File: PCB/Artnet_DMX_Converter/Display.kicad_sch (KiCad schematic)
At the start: 12 parts, among them J12 IDC

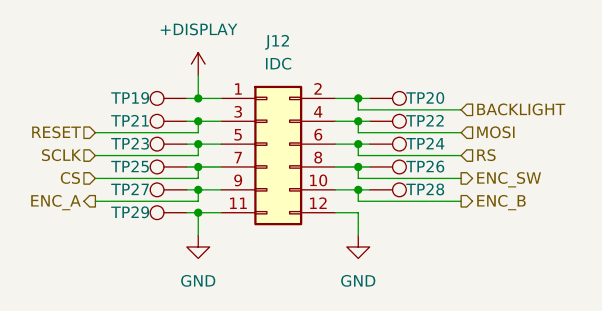
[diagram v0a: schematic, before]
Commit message: Testpoints and GND1 Fill
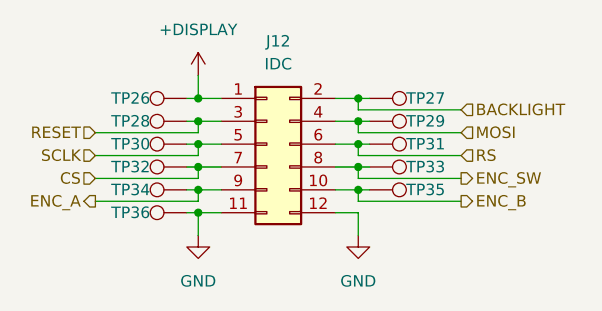
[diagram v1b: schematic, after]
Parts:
- renumbered TP19 to TP26, TP20 to TP27, TP21 to TP28, TP22 to TP29, TP23 to TP30, TP24 to TP31, TP25 to TP32, TP26 to TP33, TP27 to TP34, TP28 to TP35, TP29 to TP36
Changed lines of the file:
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@@
 		(on_board yes)
 		(dnp no)
-		(property "Reference" "TP22"
+		(property "Reference" "TP29"
 			(at 141.224 96.52 90)
 			(effects
@@
 			(project "Artnet_DMX_Converter"
 				(path "/7d5b1976-98b3-4e47-ae52-3fe360235ea3/87a5aebd-04eb-403b-8287-c063160321cf"
-					(reference "TP22")
+					(reference "TP29")
 					(unit 1)
 				)
@@
 		(on_board yes)
 		(dnp no)
-		(property "Reference" "TP19"
+		(property "Reference" "TP26"
 			(at 112.776 93.98 90)
 			(effects
@@
 			(project "Artnet_DMX_Converter"
 				(path "/7d5b1976-98b3-4e47-ae52-3fe360235ea3/87a5aebd-04eb-403b-8287-c063160321cf"
-					(reference "TP19")
+					(reference "TP26")
 					(unit 1)
 				)
@@
 		(dnp no)
 		(fields_autoplaced yes)
-		(property "Reference" "#PWR0133"
+		(property "Reference" "#PWR0138"
 			(at 118.11 115.57 0)
 			(effects
@@
 			(project "Artnet_DMX_Converter"
 				(path "/7d5b1976-98b3-4e47-ae52-3fe360235ea3/87a5aebd-04eb-403b-8287-c063160321cf"
-					(reference "#PWR0133")
+					(reference "#PWR0138")
 					(unit 1)
 				)
@@
 		(on_board yes)
 		(dnp no)
-		(property "Reference" "#PWR0132"
+		(property "Reference" "#PWR0137"
 			(at 118.11 95.25 0)
 			(effects
@@
 			(project "Artnet_DMX_Converter"
 				(path "/7d5b1976-98b3-4e47-ae52-3fe360235ea3/87a5aebd-04eb-403b-8287-c063160321cf"
-					(reference "#PWR0132")
+					(reference "#PWR0137")
 					(unit 1)
 				)
@@
 		(on_board yes)
 		(dnp no)
-		(property "Reference" "TP24"
+		(property "Reference" "TP31"
 			(at 141.224 99.06 90)
 			(effects
@@
 			(project "Artnet_DMX_Converter"
 				(path "/7d5b1976-98b3-4e47-ae52-3fe360235ea3/87a5aebd-04eb-403b-8287-c063160321cf"
-					(reference "TP24")
+					(reference "TP31")
 					(unit 1)
 				)
@@
 		(on_board yes)
 		(dnp no)
-		(property "Reference" "TP20"
+		(property "Reference" "TP27"
 			(at 141.224 93.98 90)
 			(effects
@@
 			(project "Artnet_DMX_Converter"
 				(path "/7d5b1976-98b3-4e47-ae52-3fe360235ea3/87a5aebd-04eb-403b-8287-c063160321cf"
-					(reference "TP20")
+					(reference "TP27")
 					(unit 1)
 				)
@@
 		(on_board yes)
 		(dnp no)
-		(property "Reference" "TP23"
+		(property "Reference" "TP30"
 			(at 112.776 99.06 90)
 			(effects
@@
 			(project "Artnet_DMX_Converter"
 				(path "/7d5b1976-98b3-4e47-ae52-3fe360235ea3/87a5aebd-04eb-403b-8287-c063160321cf"
-					(reference "TP23")
+					(reference "TP30")
 					(unit 1)
 				)
@@
 		(on_board yes)
 		(dnp no)
-		(property "Reference" "TP26"
+		(property "Reference" "TP33"
 			(at 141.224 101.6 90)
 			(effects
@@
 			(project "Artnet_DMX_Converter"
 				(path "/7d5b1976-98b3-4e47-ae52-3fe360235ea3/87a5aebd-04eb-403b-8287-c063160321cf"
-					(reference "TP26")
+					(reference "TP33")
 					(unit 1)
 				)
@@
 		(on_board yes)
 		(dnp no)
-		(property "Reference" "TP28"
+		(property "Reference" "TP35"
 			(at 141.224 104.14 90)
 			(effects
@@
 			(project "Artnet_DMX_Converter"
 				(path "/7d5b1976-98b3-4e47-ae52-3fe360235ea3/87a5aebd-04eb-403b-8287-c063160321cf"
-					(reference "TP28")
+					(reference "TP35")
 					(unit 1)
 				)
@@
 		(on_board yes)
 		(dnp no)
-		(property "Reference" "TP27"
+		(property "Reference" "TP34"
 			(at 112.776 104.14 90)
 			(effects
@@
 			(project "Artnet_DMX_Converter"
 				(path "/7d5b1976-98b3-4e47-ae52-3fe360235ea3/87a5aebd-04eb-403b-8287-c063160321cf"
-					(reference "TP27")
+					(reference "TP34")
 					(unit 1)
 				)
@@
 		(dnp no)
 		(fields_autoplaced yes)
-		(property "Reference" "#PWR0134"
+		(property "Reference" "#PWR0139"
 			(at 135.89 115.57 0)
 			(effects
@@
 			(project "Artnet_DMX_Converter"
 				(path "/7d5b1976-98b3-4e47-ae52-3fe360235ea3/87a5aebd-04eb-403b-8287-c063160321cf"
-					(reference "#PWR0134")
+					(reference "#PWR0139")
 					(unit 1)
 				)
@@
 		(on_board yes)
 		(dnp no)
-		(property "Reference" "TP21"
+		(property "Reference" "TP28"
 			(at 112.776 96.52 90)
 			(effects
@@
 			(project "Artnet_DMX_Converter"
 				(path "/7d5b1976-98b3-4e47-ae52-3fe360235ea3/87a5aebd-04eb-403b-8287-c063160321cf"
-					(reference "TP21")
+					(reference "TP28")
 					(unit 1)
 				)
@@
 		(on_board yes)
 		(dnp no)
-		(property "Reference" "TP29"
+		(property "Reference" "TP36"
 			(at 112.776 106.68 90)
 			(effects
@@
 			(project "Artnet_DMX_Converter"
 				(path "/7d5b1976-98b3-4e47-ae52-3fe360235ea3/87a5aebd-04eb-403b-8287-c063160321cf"
-					(reference "TP29")
+					(reference "TP36")
 					(unit 1)
 				)
@@
 		(on_board yes)
 		(dnp no)
-		(property "Reference" "TP25"
+		(property "Reference" "TP32"
 			(at 112.776 101.6 90)
 			(effects
@@
 			(project "Artnet_DMX_Converter"
 				(path "/7d5b1976-98b3-4e47-ae52-3fe360235ea3/87a5aebd-04eb-403b-8287-c063160321cf"
-					(reference "TP25")
-					(unit 1)
-				)
+					(reference "TP32")
+					(unit 1)
+				)
